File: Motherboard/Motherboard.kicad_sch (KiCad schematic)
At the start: 53 parts, among them J1 Conn_01x01, J10 ATX-24, J11 USB_B, J12 Bus_ISA_8bit, J13 65SIB_Connector, J2 Conn_01x01, J3 Conn_01x01, J4 Conn_01x01, J5 Conn_01x01, J6 Conn_01x01, J7 Conn_01x01, J8 Conn_01x01, J9 Bus_ISA_8bit, SW1 SW_Push, SW2 SW_SPST, U1 SC28L91, U10 XCR3064XL-VQ100, U11 XCR3064-VQ100, U12 LM7905_TO220, U13 MCP2200-I-SO, U14 74HCT163, U15 74HCT137, U2 AS6C1608, U3 WD65C22, U4 SST39SF040, U5 SST39SF040, U6 WD65C816S, U7 DS1813, U8 74HCT245, U9 74HCT573, X1 ACO-3.6864MHz, X2 ACO-24MHz, X3 ACO-14.31818MHz

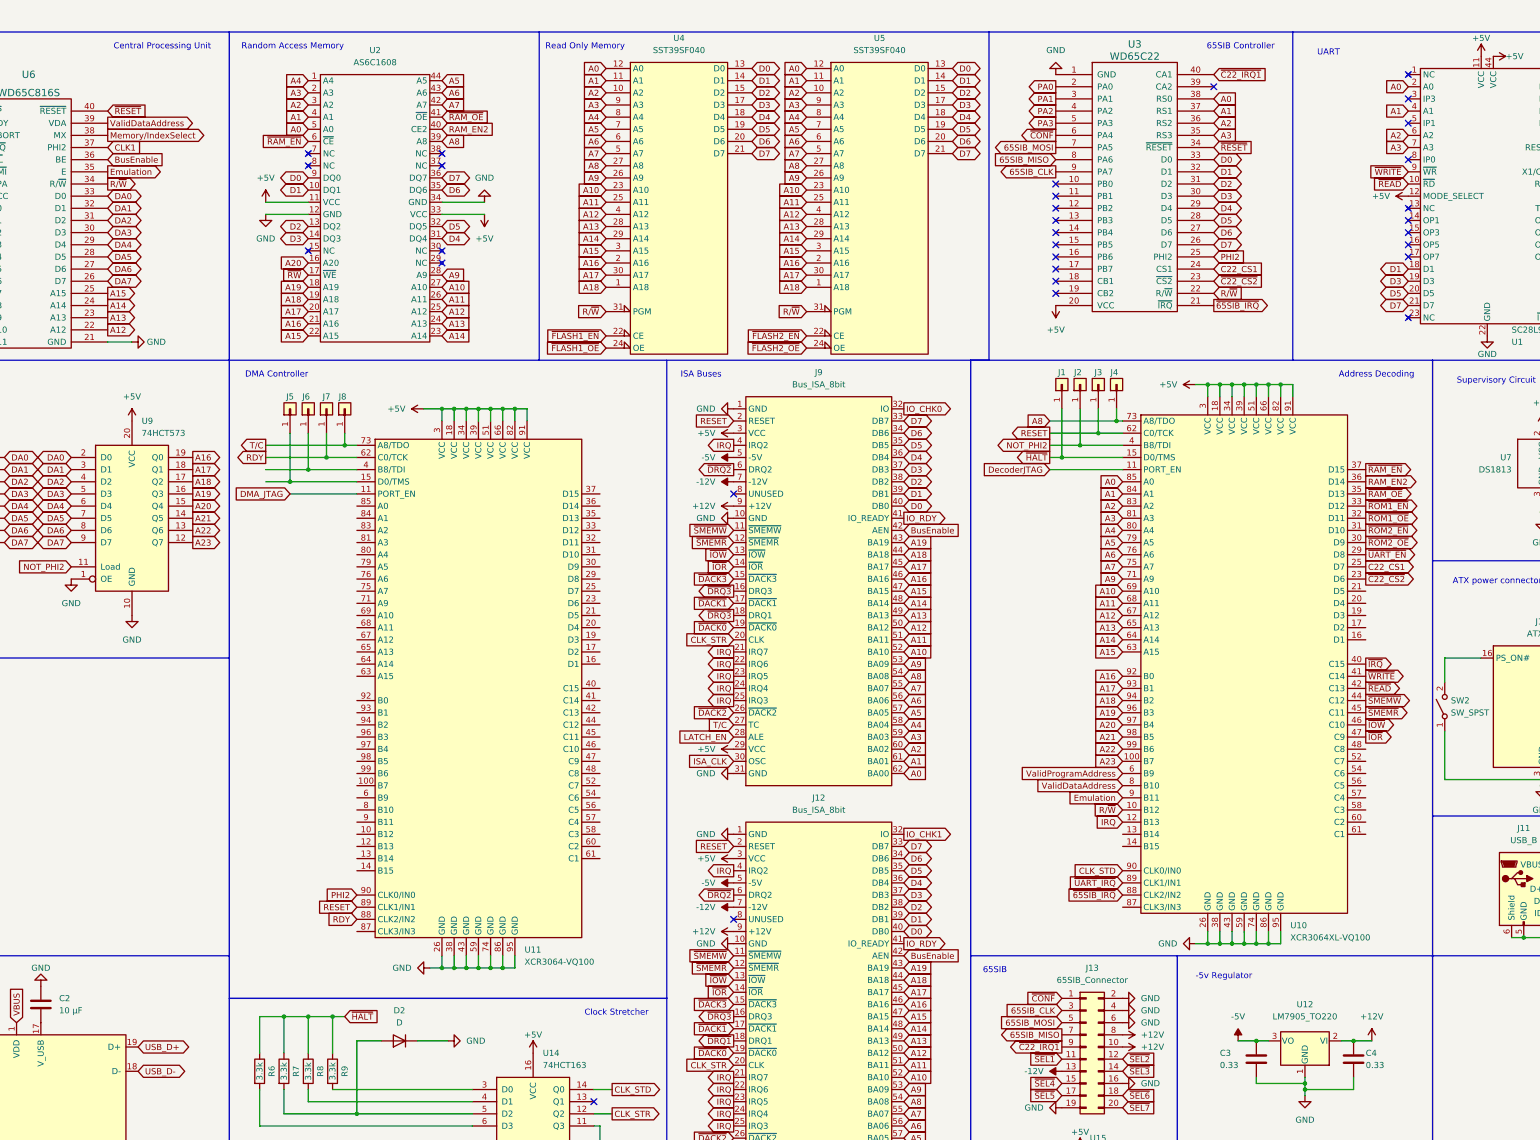
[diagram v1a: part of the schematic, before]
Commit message: Update Motherboard.kicad_sch
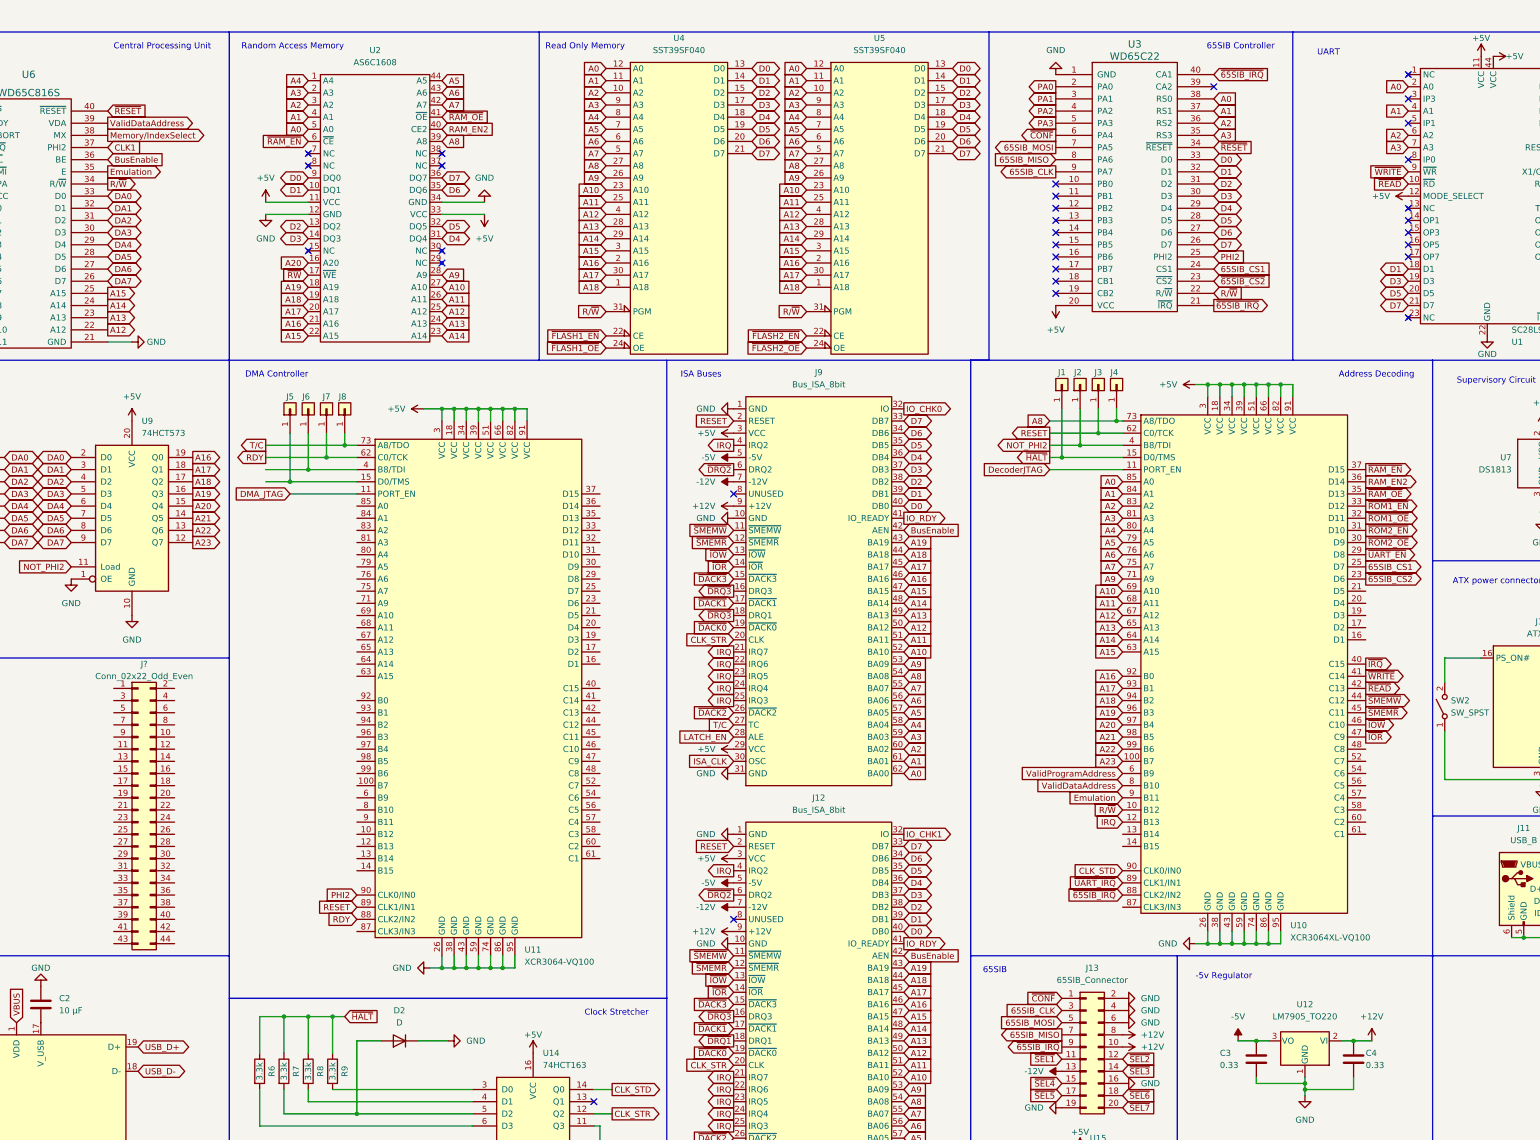
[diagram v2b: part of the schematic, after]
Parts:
- added J?: Conn_02x22_Odd_Even, symbol Connector_Generic:Conn_02x22_Odd_Even
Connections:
- net ~{C22_IRQ1} is gone; now on net ~{65SIB_IRQ}: J13.9 (IRO\), U3.40 (CA1)
- net C22_CS1: no longer U10.25 (D7), U3.24 (CS1)
- net ~{C22_CS2}: no longer U10.23 (D6), U3.23 (~{CS2})
- new net 65SIB_CS1: U10.25 (D7), U3.24 (CS1)
- new net ~{65SIB_CS2}: U10.23 (D6), U3.23 (~{CS2})
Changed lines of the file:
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@@
     )
   )
-  (global_label "C22_CS1" (shape output) (at 336.55 127 0) (fields_autoplaced)
+  (global_label "65SIB_CS1" (shape output) (at 336.55 127 0) (fields_autoplaced)
     (effects (font (size 1.27 1.27)) (justify left))
-    (property "Intersheet References" "${INTERSHEET_REFS}" (id 0) (at 347.3088 126.9206 0)
+    (property "Intersheet References" "${INTERSHEET_REFS}" (id 0) (at 349.1231 126.9206 0)
       (effects (font (size 1.27 1.27)) (justify left) hide)
     )
@@
     )
   )
-  (global_label "C22_CS1" (shape input) (at 304.8 64.77 0) (fields_autoplaced)
+  (global_label "65SIB_CS1" (shape input) (at 304.8 64.77 0) (fields_autoplaced)
     (effects (font (size 1.27 1.27)) (justify left))
-    (property "Intersheet References" "${INTERSHEET_REFS}" (id 0) (at 315.5588 64.6906 0)
+    (property "Intersheet References" "${INTERSHEET_REFS}" (id 0) (at 317.3731 64.6906 0)
       (effects (font (size 1.27 1.27)) (justify left) hide)
     )
@@
     )
   )
-  (global_label "~{C22_CS2}" (shape input) (at 304.8 67.31 0) (fields_autoplaced)
+  (global_label "~{65SIB_CS2}" (shape input) (at 304.8 67.31 0) (fields_autoplaced)
     (effects (font (size 1.27 1.27)) (justify left))
-    (property "Intersheet References" "${INTERSHEET_REFS}" (id 0) (at 315.5588 67.2306 0)
+    (property "Intersheet References" "${INTERSHEET_REFS}" (id 0) (at 317.3731 67.2306 0)
       (effects (font (size 1.27 1.27)) (justify left) hide)
     )
@@
     )
   )
-  (global_label "~{C22_IRQ1}" (shape output) (at 273.05 227.33 180) (fields_autoplaced)
+  (global_label "~{65SIB_IRQ}" (shape output) (at 273.05 227.33 180) (fields_autoplaced)
     (effects (font (size 1.27 1.27)) (justify right))
-    (property "Intersheet References" "${INTERSHEET_REFS}" (id 0) (at 261.5655 227.2506 0)
+    (property "Intersheet References" "${INTERSHEET_REFS}" (id 0) (at 260.9607 227.2506 0)
       (effects (font (size 1.27 1.27)) (justify right) hide)
     )
@@
     )
   )
-  (global_label "~{C22_CS2}" (shape output) (at 336.55 129.54 0) (fields_autoplaced)
+  (global_label "~{65SIB_CS2}" (shape output) (at 336.55 129.54 0) (fields_autoplaced)
     (effects (font (size 1.27 1.27)) (justify left))
-    (property "Intersheet References" "${INTERSHEET_REFS}" (id 0) (at 347.3088 129.4606 0)
+    (property "Intersheet References" "${INTERSHEET_REFS}" (id 0) (at 349.1231 129.4606 0)
       (effects (font (size 1.27 1.27)) (justify left) hide)
     )
@@
     )
   )
-  (global_label "~{C22_IRQ1}" (shape input) (at 304.8 24.13 0) (fields_autoplaced)
+  (global_label "~{65SIB_IRQ}" (shape input) (at 304.8 24.13 0) (fields_autoplaced)
     (effects (font (size 1.27 1.27)) (justify left))
-    (property "Intersheet References" "${INTERSHEET_REFS}" (id 0) (at 316.2845 24.2094 0)
+    (property "Intersheet References" "${INTERSHEET_REFS}" (id 0) (at 316.8893 24.0506 0)
       (effects (font (size 1.27 1.27)) (justify left) hide)
     )
@@
     (pin "9")
   )
+  (symbol (lib_id "Connector_Generic:Conn_02x22_Odd_Even") (at 80.01 177.8 0) (unit 1)
+    (in_bom yes) (on_board yes)
+    (property "Reference" "J?" (id 0) (at 81.28 147.32 0))
+    (property "Value" "Conn_02x22_Odd_Even" (id 1) (at 81.28 149.86 0))
+    (property "Footprint" "" (id 2) (at 80.01 177.8 0)
+      (effects (font (size 1.27 1.27)) hide)
+    )
+    (property "Datasheet" "~" (id 3) (at 80.01 177.8 0)
+      (effects (font (size 1.27 1.27)) hide)
+    )
+    (pin "1")
+    (pin "10")
+    (pin "11")
+    (pin "12")
+    (pin "13")
+    (pin "14")
+    (pin "15")
+    (pin "16")
+    (pin "17")
+    (pin "18")
+    (pin "19")
+    (pin "2")
+    (pin "20")
+    (pin "21")
+    (pin "22")
+    (pin "23")
+    (pin "24")
+    (pin "25")
+    (pin "26")
+    (pin "27")
+    (pin "28")
+    (pin "29")
+    (pin "3")
+    (pin "30")
+    (pin "31")
+    (pin "32")
+    (pin "33")
+    (pin "34")
+    (pin "35")
+    (pin "36")
+    (pin "37")
+    (pin "38")
+    (pin "39")
+    (pin "4")
+    (pin "40")
+    (pin "41")
+    (pin "42")
+    (pin "43")
+    (pin "44")
+    (pin "5")
+    (pin "6")
+    (pin "7")
+    (pin "8")
+    (pin "9")
+  )
   (symbol (lib_id "Connector_Generic:Conn_01x01") (at 280.67 88.9 90) (unit 1)
     (in_bom yes) (on_board yes)
@@
       (reference "J13") (unit 1) (value "65SIB_Connector") (footprint "")
     )
+    (path "/82ae432e-c3a9-4411-b1b3-31982e3567a0"
+      (reference "J?") (unit 1) (value "Conn_02x22_Odd_Even") (footprint "")
+    )
     (path "/4a1e7941-057e-4480-9338-181046145fde"

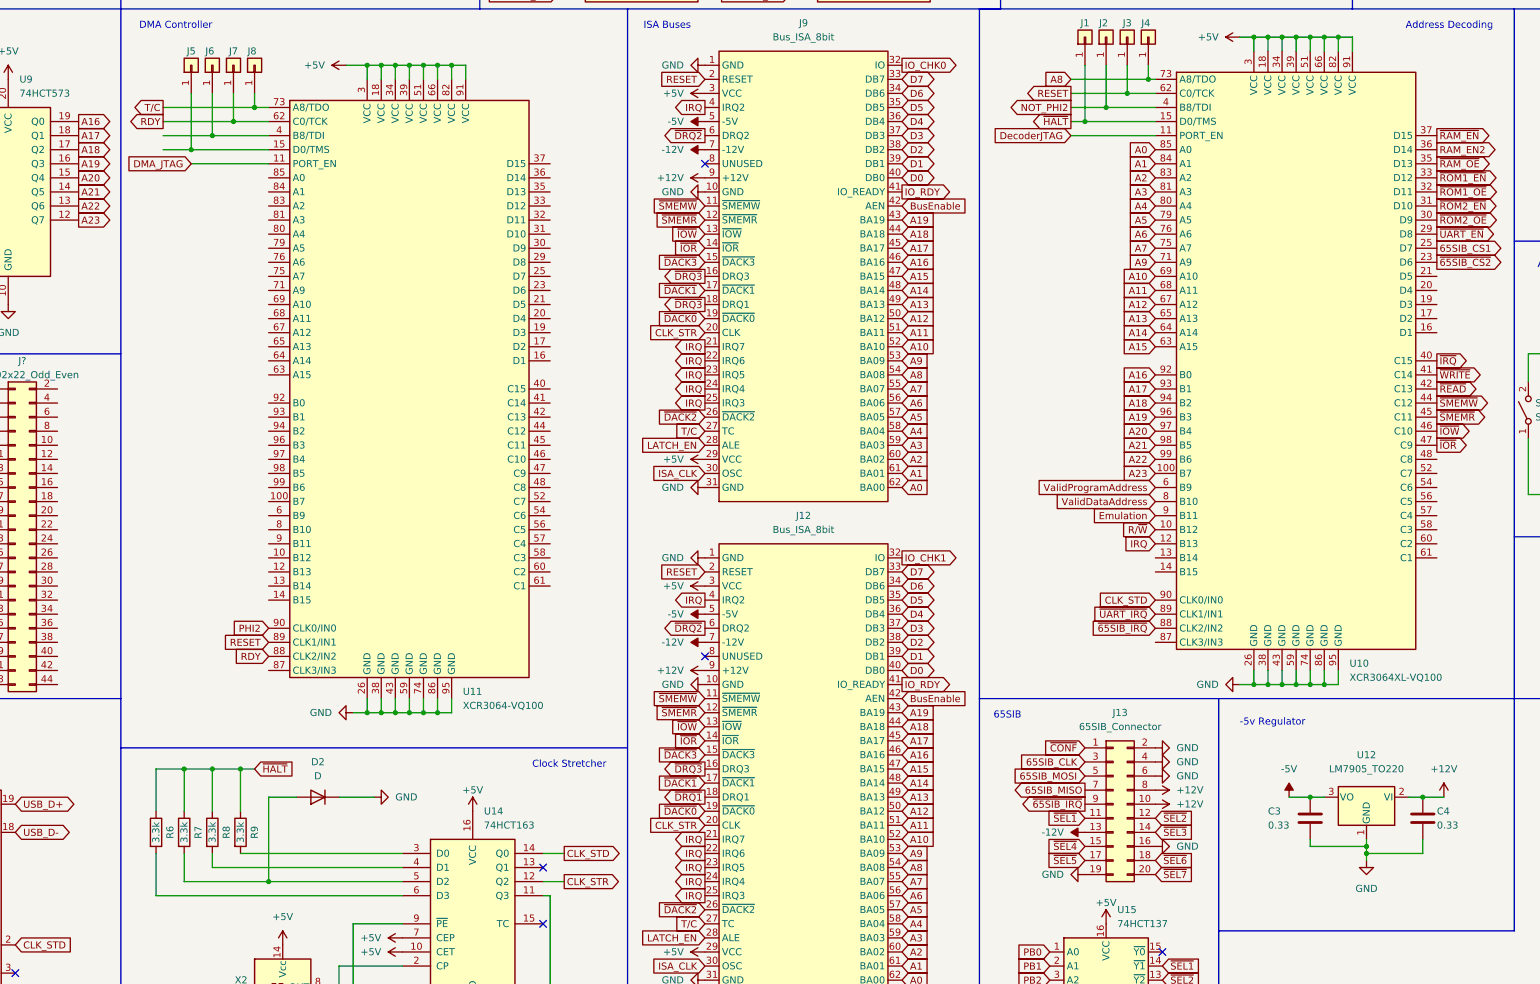
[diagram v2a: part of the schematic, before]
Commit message: Finished schematic for address decoding...
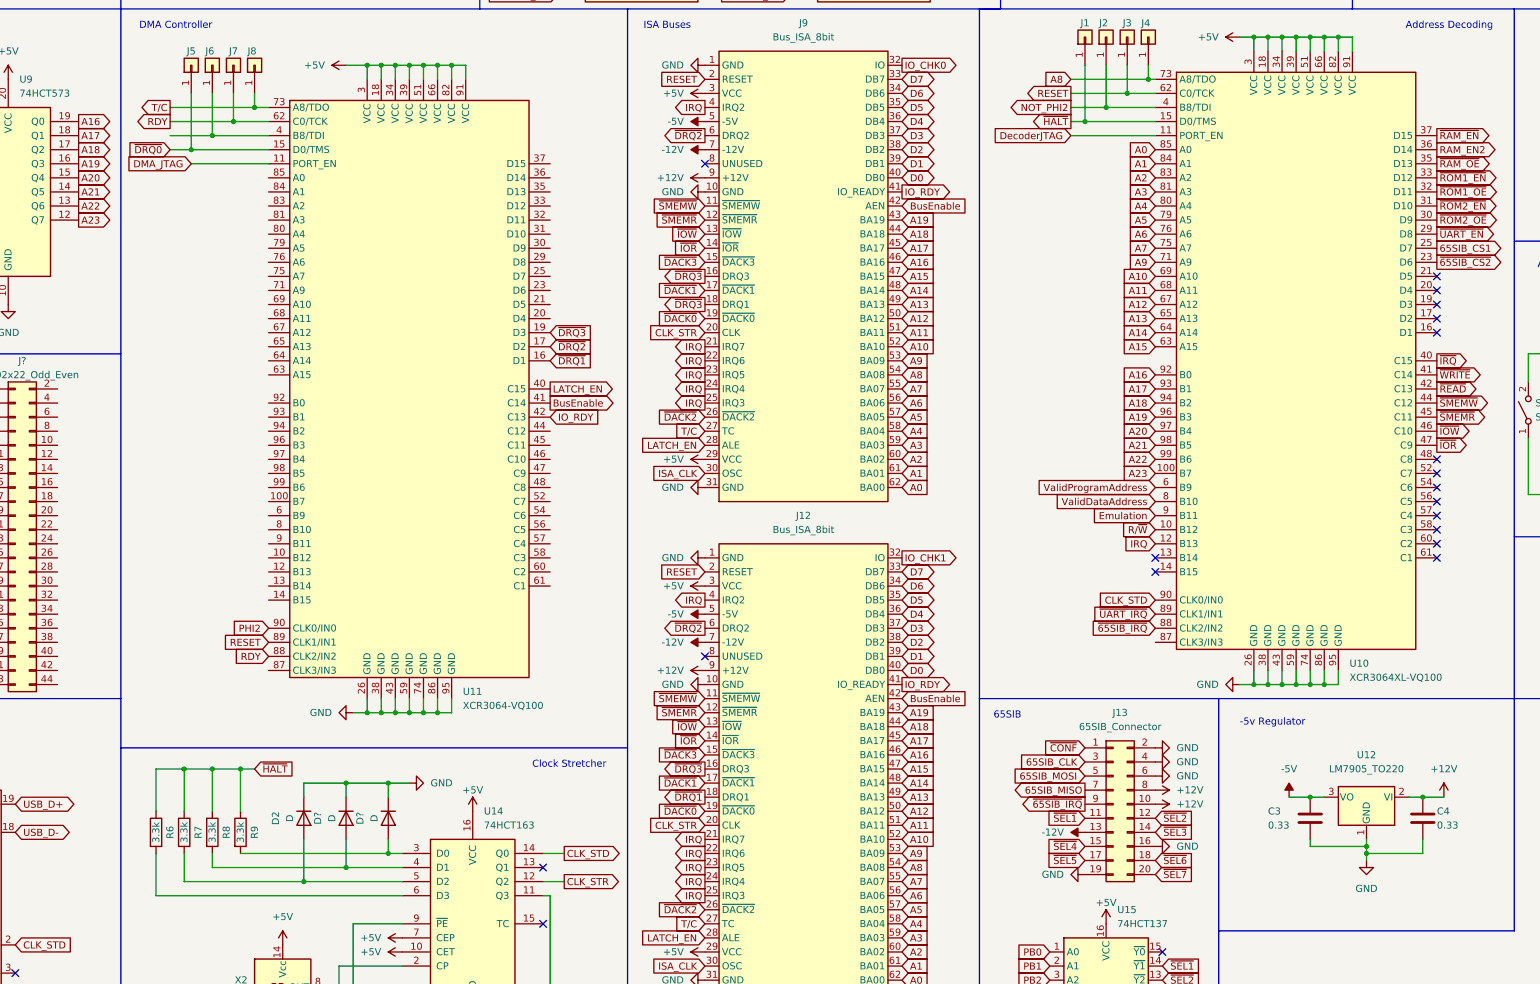
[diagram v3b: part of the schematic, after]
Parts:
- added D? (x2): D, Diode_THT:D_A-405_P7.62mm_Horizontal, symbol Device:D
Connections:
- net BusEnable: now also U11.41 (C14)
- net GND: now also D?.1 (K), D?.1 (K)
- net IO_RDY: now also U11.42 (C13)
- net LATCH_EN: now also U11.40 (C15)
- net ~{DRQ1}: now also U11.16 (D1)
- net ~{DRQ2}: now also U11.17 (D2)
- net ~{DRQ3}: now also U11.19 (D3)
- net at R9.2, U14.3 (D0): now also D?.2 (A)
- net at R8.2, U14.4 (D1): now also D?.2 (A)
- net ~{DRQ0}: now reaches J5.1 (Pin_1), U11.15 (D0/TMS)
- no-connect marks 55 -> 70
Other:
- moved on the sheet: D2
